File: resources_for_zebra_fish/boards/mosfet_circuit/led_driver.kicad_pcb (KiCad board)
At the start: 2 copper layers, 67.3 x 33 mm, 11 parts, among them J1 Vin, J2 control_in, J4 LED, Q1 N_chan_mosfet, Q2 P-Chan_mosfet

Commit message: clean up mosfet circuit
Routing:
- net Net-(Q2-Pad5): track 45.0 -> 3.81 mm, vias 1 -> 0
- net Net-(J4-Pad1): track 36.9 -> 0.00 mm
- net Net-(J1-Pad1): track 34.1 -> 14.4 mm
- net Net-(Q1-Pad5): track 51.9 -> 45.7 mm
- added copper zone on F.Cu, net Net-(J1-Pad1)
- added copper zone on B.Cu, net Net-(J4-Pad1)
- added copper zone on F.Cu, net Net-(Q1-Pad5)
- added copper zone on F.Cu, net Net-(Q2-Pad5)
- added copper zone on F.Cu, net Net-(R4-Pad1)

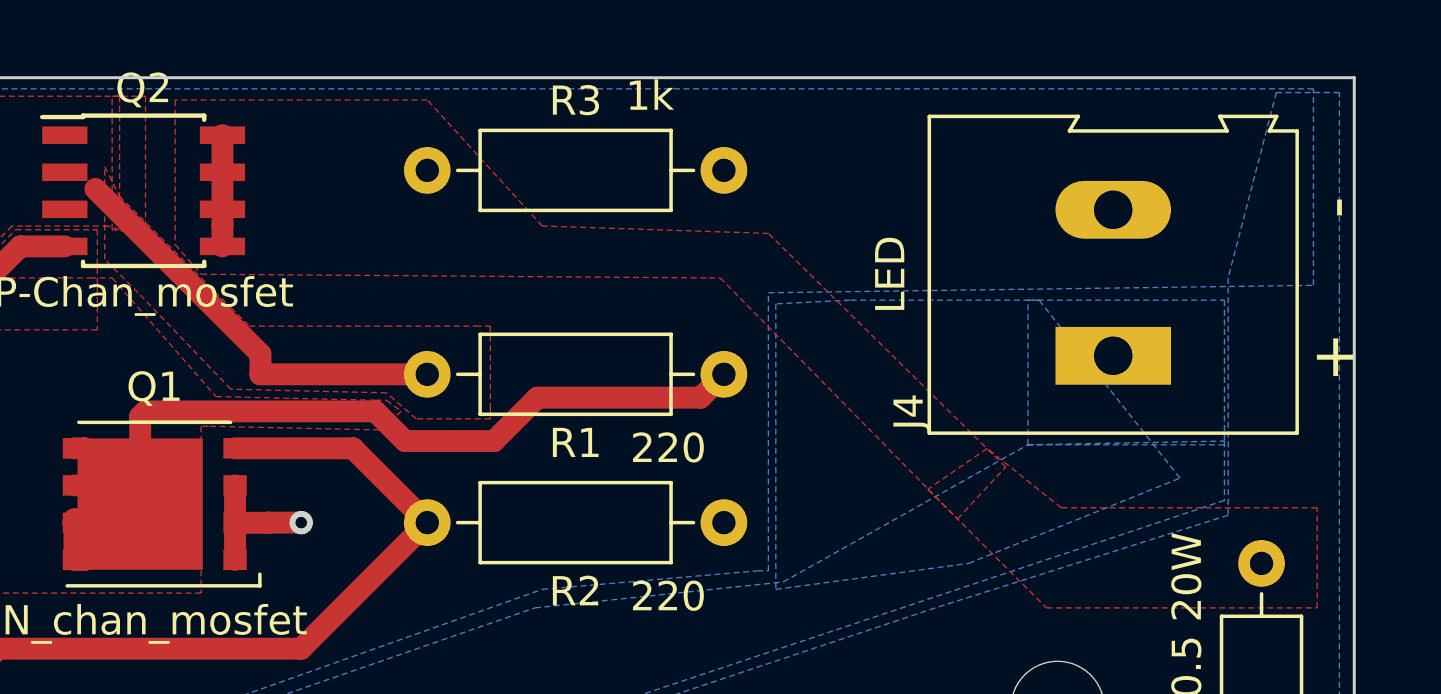
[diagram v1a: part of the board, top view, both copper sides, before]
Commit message: new board: power supply and sync to led in one
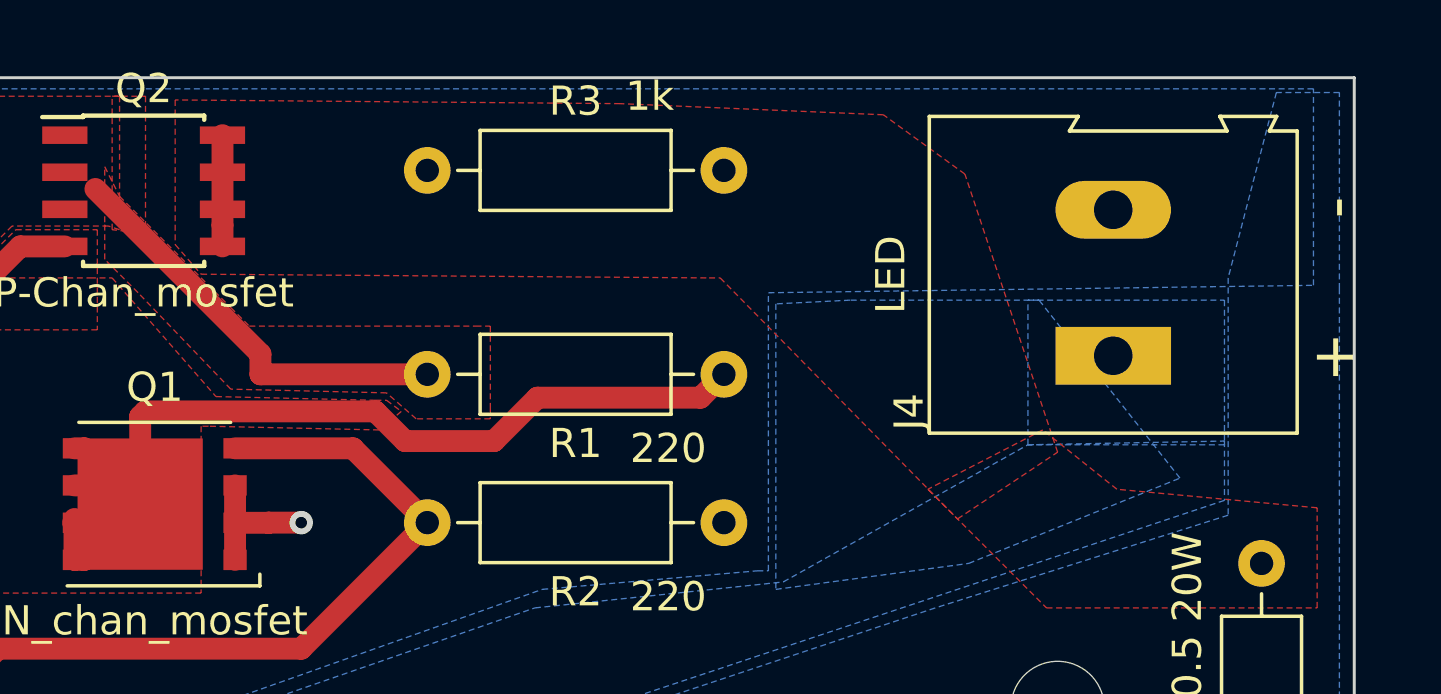
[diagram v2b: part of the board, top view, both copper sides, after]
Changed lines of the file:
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@@
       (pts
         (xy 185.674 69.342) (xy 185.674 74.295) (xy 186.563 75.311) (xy 203.962 75.438) (xy 204.343 75.438)
-        (xy 212.471 83.693) (xy 214.122 81.915) (xy 205.994 73.914) (xy 198.247 73.66) (xy 194.31 69.342)
+        (xy 212.471 83.693) (xy 215.9 81.407) (xy 212.725 71.882) (xy 209.931 69.85) (xy 200.914 69.469)
       )
     )
@@
     (polygon
       (pts
-        (xy 211.455 82.677) (xy 215.519 86.741) (xy 224.79 86.741) (xy 224.79 83.312) (xy 216.027 83.312)
-        (xy 213.487 81.28)
+        (xy 211.455 82.677) (xy 215.519 86.741) (xy 224.79 86.741) (xy 224.79 83.312) (xy 217.932 82.677)
+        (xy 215.392 80.645)
       )
     )
